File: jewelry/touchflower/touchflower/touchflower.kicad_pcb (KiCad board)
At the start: 2 copper layers, 5 parts, among them J1 Conn_01x03, U1 TPP223-BA6

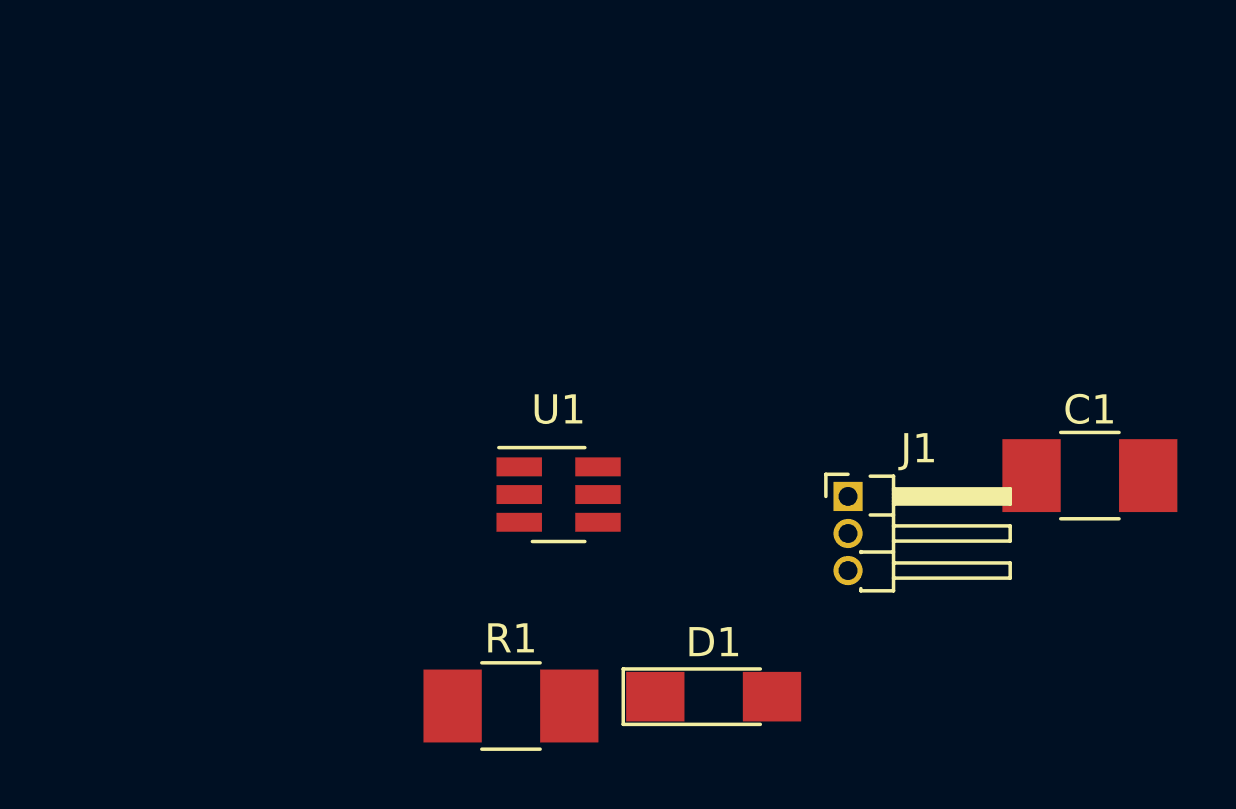
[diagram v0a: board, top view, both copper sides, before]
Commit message: jewelry: Initial PCB layout
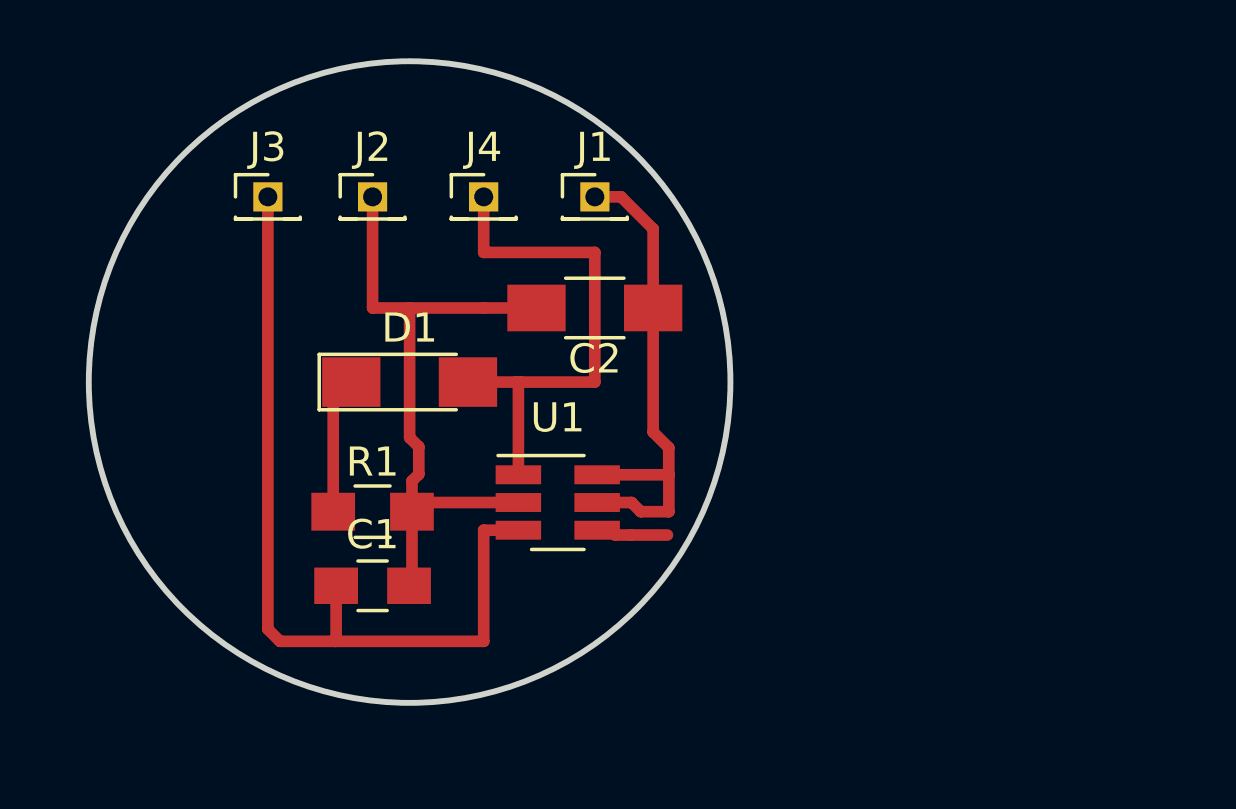
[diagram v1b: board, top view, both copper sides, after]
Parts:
- added C2: CP, Capacitors_SMD:C_1206_HandSoldering, F.Cu at (6.35, -2.54)
- added J2: Conn_01x01, Pin_Headers:Pin_Header_Straight_1x01_Pitch1.27mm, F.Cu at (-1.27, -6.35)
- added J3: Conn_01x01, Pin_Headers:Pin_Header_Straight_1x01_Pitch1.27mm, F.Cu at (-4.86, -6.35)
- added J4: Conn_01x01, Pin_Headers:Pin_Header_Straight_1x01_Pitch1.27mm, F.Cu at (2.54, -6.35)
- C1: footprint Capacitors_SMD:C_1210_HandSoldering -> Capacitors_SMD:C_0805_HandSoldering
- J1: value Conn_01x03 -> Conn_01x01; footprint Pin_Headers:Pin_Header_Angled_1x03_Pitch1.27mm -> Pin_Headers:Pin_Header_Straight_1x01_Pitch1.27mm
- R1: footprint Resistors_SMD:R_1210_HandSoldering -> Resistors_SMD:R_0805_HandSoldering
- moved C1 24.9 mm to (-1.27, 6.99)
- moved D1 15.0 mm to (0.00, 0.00)
- moved J1 13.5 mm to (6.35, -6.35)
- moved R1 8.18 mm to (-1.27, 4.45)
- moved U1 0.27 mm to (5.08, 4.13)
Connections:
- net Net-(D1-Pad2) renamed /out
- C1 pad 1: /touch -> /sensor
- U1 pad 3: /touch -> /sensor
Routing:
- net /sensor: track 0.00 -> 29.3 mm
- net GND: track 0.00 -> 23.8 mm
- net /out: track 0.00 -> 17.7 mm
- net VDD: track 0.00 -> 17.6 mm
- net Net-(D1-Pad1): track 0.00 -> 4.70 mm
- net Net-(U1-Pad4): track 0.00 -> 2.48 mm
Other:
- board outline added: 22 x 22 mm
- net class Default: clearance 0.2 -> 0.4; trace_width 0.25 -> 0.4
- rule trace_clearance: 0.2 -> 0.4
- rule trace_min: 0.2 -> 0.4

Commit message: touchflower: Add battery holder for CR2032
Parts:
- added BT1: Battery_Cell, touchflower:BK-913, B.Cu at (0.01, 0.00)
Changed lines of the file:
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@@
     (tracks 48)
     (zones 0)
-    (modules 9)
+    (modules 10)
     (nets 7)
   )
@@
     )
   )
+  (module touchflower:BK-913 (layer B.Cu)
+    (at 0.005 0)
+    (fp_text reference BT1 (at 0 -0.5) (layer B.SilkS)
+      (effects (font (size 1 1) (thickness 0.15)) (justify mirror))
+    )
+    (fp_text value Battery_Cell (at 0 0.5) (layer B.Fab)
+      (effects (font (size 1 1) (thickness 0.15)) (justify mirror))
+    )
+    (fp_circle (center 0 0) (end 10 0) (layer B.CrtYd) (width 0.15))
+    (fp_line (start -10.75 7.75) (end 10.75 7.75) (layer B.Fab) (width 0.15))
+    (fp_line (start 10.75 7.75) (end 10.75 -7.75) (layer B.Fab) (width 0.15))
+    (fp_line (start 10.75 -7.75) (end -10.75 -7.75) (layer B.Fab) (width 0.15))
+    (fp_line (start -10.75 -7.75) (end -10.75 7.75) (layer B.Fab) (width 0.15))
+    (pad 1 thru_hole circle (at 10.8 0) (size 2.5 2.5) (drill 2) (layers *.Cu *.Mask)
+      (net 3 VDD))
+    (pad 1 thru_hole circle (at -10.8 0) (size 2.5 2.5) (drill 2) (layers *.Cu *.Mask)
+      (net 3 VDD))
+    (pad 2 smd rect (at 0 0) (size 3.96 3.96) (layers B.Cu B.Paste B.Mask)
+      (net 1 GND))
+  )
   (gr_circle (center 0 0) (end 7 0) (layer Eco1.User) (width 0.2))

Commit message: touchflower: Custom SOT223-6
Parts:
- U1: footprint TO_SOT_Packages_SMD:SOT-23-6_Handsoldering -> touchflower:SOT-223-6-extraspace
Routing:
- net VDD: track 17.6 -> 19.5 mm
- net GND: track 23.8 -> 23.6 mm, vias 0 -> 2
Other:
- net class Default: via_dia 0.8 -> 1.2; via_drill 0.4 -> 0.8
